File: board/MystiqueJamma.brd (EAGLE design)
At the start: 120 x 145 mm, 36 parts, among them IC1 7805, IC2 74LS245N, IC3 74LS245N, IC4 74LS245N, IC5 CY7C1049CV33

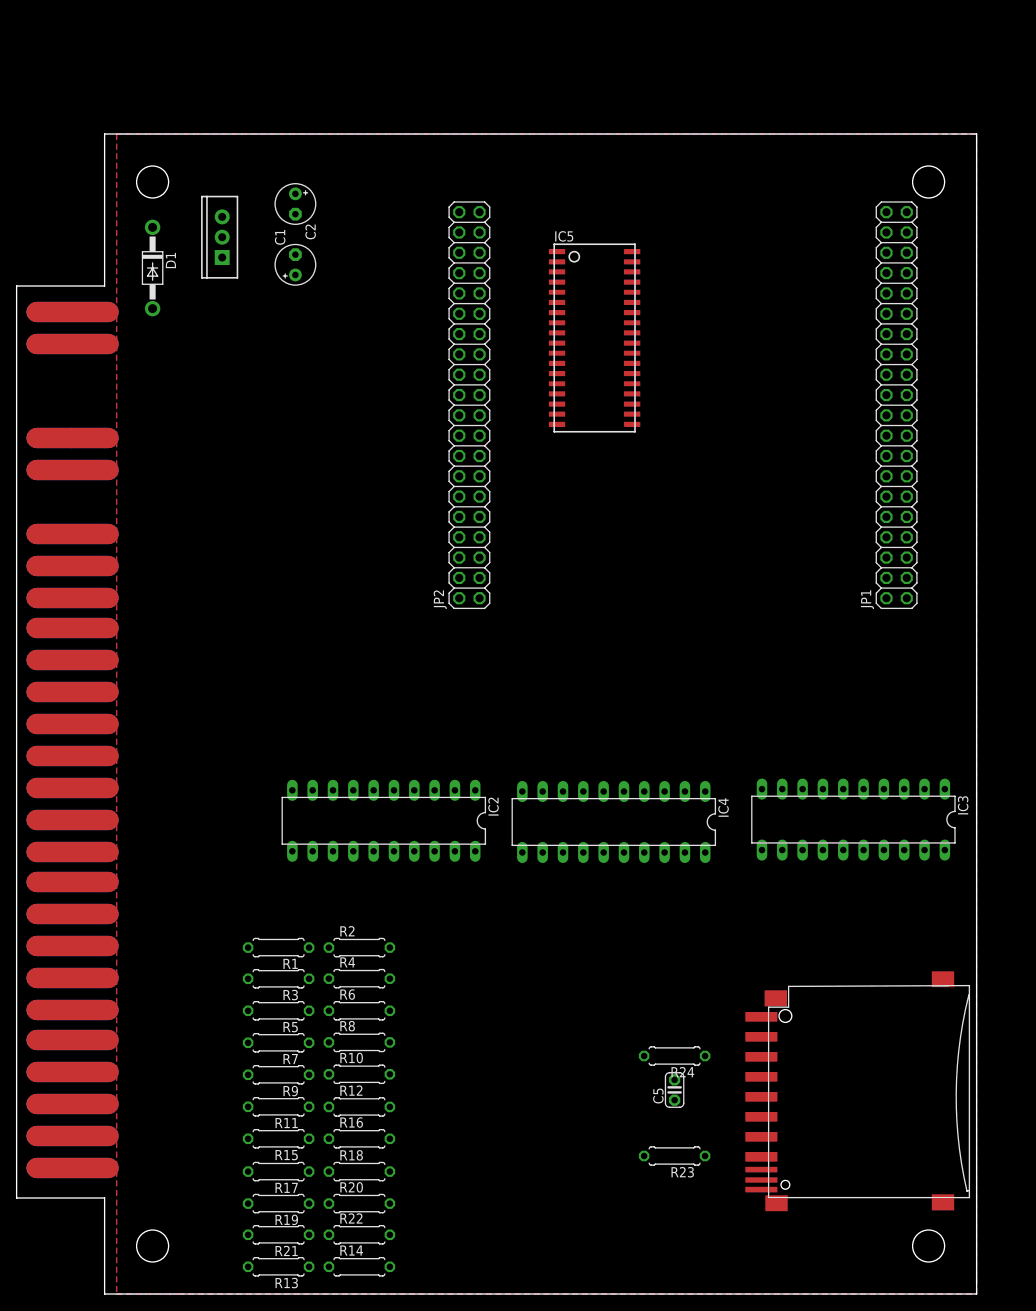
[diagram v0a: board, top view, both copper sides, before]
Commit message: changed the jamma connector and included audio TDA1543
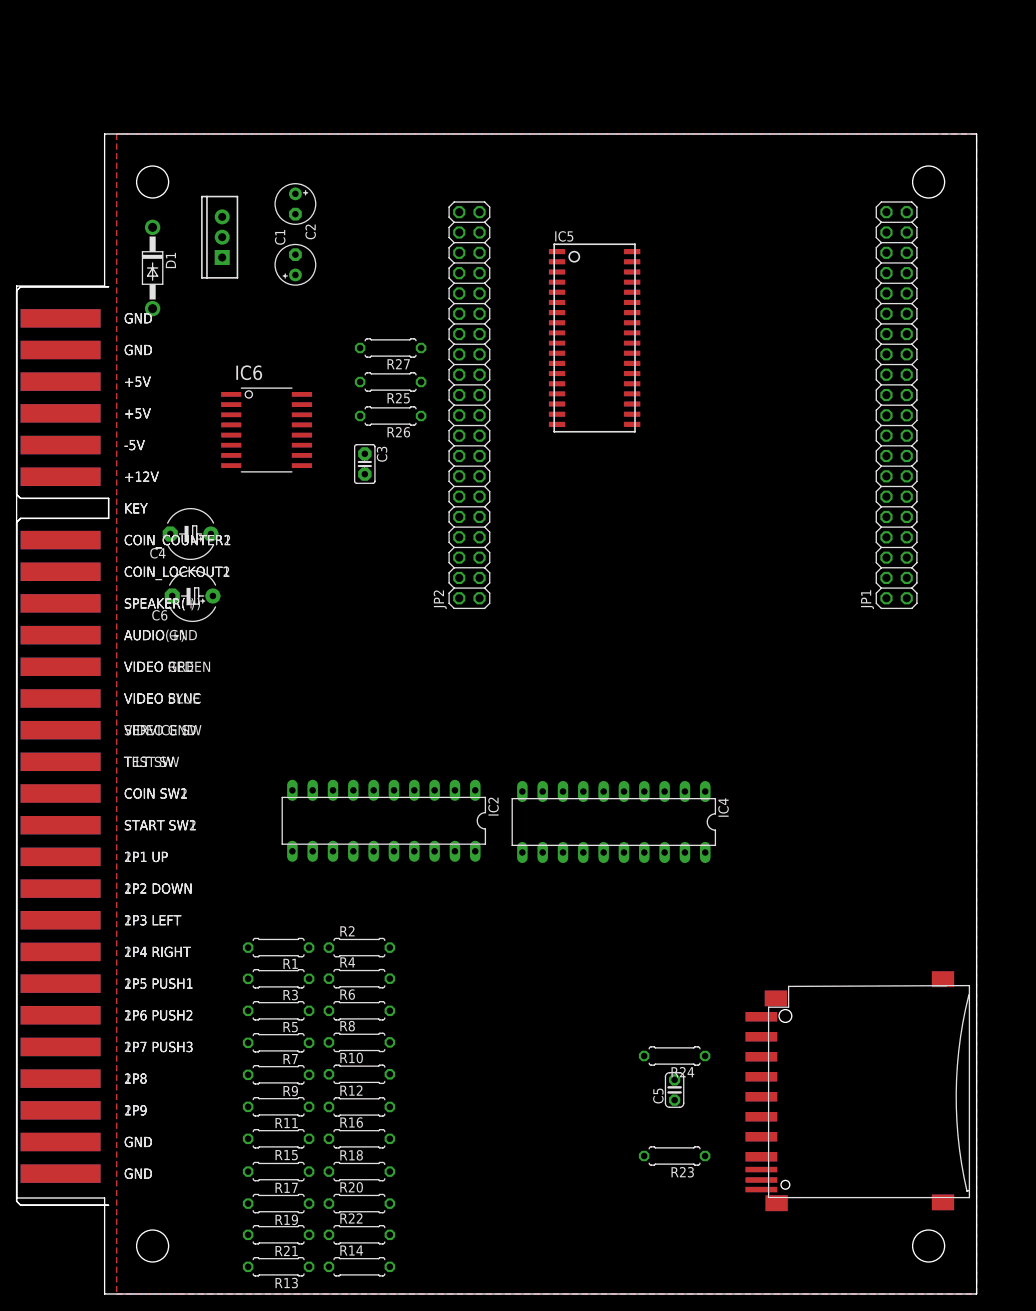
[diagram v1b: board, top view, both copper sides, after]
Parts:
- removed IC3: 74LS245N, 74xx-us:DIL20
- added C3: 100nF, adafruit:C025-025X050
- added C4, C6: 4.7uF, adafruit:E5-6
- added IC6: TDA1543T, TDA1543:SOIC-16NW
- added JAMMA1: JAMMA_TOP, JAMMA:JAMMA_TOP
- added JAMMA2: JAMMA_BOTTOM, JAMMA:JAMMA_BOTTOM
- added R25: 1k, adafruit:0207/7
- added R26, R27: 2k, adafruit:0207/7
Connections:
- removed net CS2_: IC3.18
- removed net CS2_3V: IC3.2
- removed net P2B1_: IC3.12
- removed net P2B1_3V: IC3.8
- removed net P2B2_: IC3.11
- removed net P2B2_3V: IC3.9
- removed net P2B3_: IC4.15
- removed net P2B3_3V: IC4.5
- removed net P2B4_: IC4.14
- removed net P2B4_3V: IC4.6
- removed net P2B5_: IC4.13
- removed net P2B5_3V: IC4.7
- removed net P2D_: IC3.15
- removed net P2D_3V: IC3.5
- removed net P2L_: IC3.14
- removed net P2L_3V: IC3.6
- removed net P2R_: IC3.13
- removed net P2R_3V: IC3.7
- removed net P2S_: IC3.17
- removed net P2S_3V: IC3.3
- removed net P2U_: IC3.16
- removed net P2U_3V: IC3.4
- new net +5V: JAMMA1.3, JAMMA1.4, JAMMA2.C, JAMMA2.D
- new net -5V: JAMMA1.5, JAMMA2.E
- new net 12+: JAMMA2.F
- new net DAC_DATA: IC6.5
- new net DAC_FSYNC: IC6.4
- new net DAC_SCK: IC6.3
- new net DAC_VREF: IC6.13, R25.2
- new net L_A: C6.+, IC6.12, R26.2
- new net L_AUDIO: C6.-
- new net R_A: C4.+, IC6.14, R27.2
- new net R_AUDIO: C4.-
- net +12: now also JAMMA1.6
- net +3V3: no longer IC3.20
- net +5REG: now also C3.1, IC6.11
- net COINSW1: now also JAMMA1.16
- net GND: now also C3.2, IC6.6, JAMMA1.1, JAMMA1.2, JAMMA1.27, JAMMA1.28, JAMMA2.A, JAMMA2.B, JAMMA2._E, JAMMA2._F, R25.1, R26.1, R27.1; no longer IC3.1, IC3.10, IC3.19
- net P1B1: now also JAMMA1.22
- net P1B2: now also JAMMA1.23
- net P1B3: now also JAMMA1.24
- net P1B4: now also JAMMA1.25
- net P1B5: now also JAMMA1.26
- net P1DW: now also JAMMA1.19
- net P1LH: now also JAMMA1.20
- net P1RH: now also JAMMA1.21
- net P1START: now also JAMMA1.17
- net P1UP: now also JAMMA1.18
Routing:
- net GND: track 72.0 -> 0.00 mm
- net -5: track 18.0 -> 0.00 mm
- net +12: track 18.0 -> 0.00 mm
- net VIDEOSYN: track 9.00 -> 0.00 mm
- net VIDEORED: track 9.00 -> 0.00 mm
- net VIDEOGR: track 9.00 -> 0.00 mm
- net VIDEOGND: track 9.00 -> 0.00 mm
- net VIDEOBLUE: track 9.00 -> 0.00 mm
- net TILTSW: track 9.00 -> 0.00 mm
- net TESTSW: track 9.00 -> 0.00 mm
- net SPEAKER-: track 9.00 -> 0.00 mm
- net SPEAKER+: track 9.00 -> 0.00 mm
- net SERVSW: track 9.00 -> 0.00 mm
- net S$11: track 9.00 -> 0.00 mm
- net P2UP: track 9.00 -> 0.00 mm
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
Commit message: audio circuit update
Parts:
- added R28, R29: 1k, adafruit:0207/7
- moved C4 14.3 mm to (34.8, 89.0)
- moved C6 14.2 mm to (35.0, 81.5)
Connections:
- new net JAMMA_SPK+: JAMMA1.10, R28.2, R29.2
- net GND: now also JAMMA2.L
- net L_AUDIO: now also R29.1
- net R_AUDIO: now also R28.1
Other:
- outline, holes or cut-outs redrawn
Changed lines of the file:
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@@
 <board>
 <plain>
-<wire x1="0" y1="12" x2="0" y2="126" width="0.1524" layer="20"/>
-<wire x1="11" y1="145" x2="120" y2="145" width="0.1524" layer="20"/>
+<wire x1="0" y1="11" x2="0" y2="126" width="0.1524" layer="20"/>
+<wire x1="11.5" y1="145" x2="120" y2="145" width="0.1524" layer="20"/>
 <wire x1="120" y1="145" x2="120" y2="0" width="0.1524" layer="20"/>
-<wire x1="120" y1="0" x2="11" y2="0" width="0.1524" layer="20"/>
-<wire x1="11" y1="0" x2="11" y2="12" width="0.1524" layer="20"/>
-<wire x1="11" y1="12" x2="0" y2="12" width="0.1524" layer="20"/>
-<wire x1="0" y1="126" x2="11" y2="126" width="0.1524" layer="20"/>
-<wire x1="11" y1="126" x2="11" y2="145" width="0.1524" layer="20"/>
+<wire x1="120" y1="0" x2="11.5" y2="0" width="0.1524" layer="20"/>
+<wire x1="11.5" y1="0" x2="11.5" y2="11" width="0.1524" layer="20"/>
+<wire x1="11.5" y1="11" x2="0" y2="11" width="0.1524" layer="20"/>
+<wire x1="0" y1="126" x2="11.5" y2="126" width="0.1524" layer="20"/>
+<wire x1="11.5" y1="126" x2="11.5" y2="145" width="0.1524" layer="20"/>
 <hole x="17" y="6" drill="4"/>
 <hole x="114" y="6" drill="4"/>
@@
 <element name="C3" library="adafruit" package="C025-025X050" value="100nF" x="43.5242" y="103.75" rot="R270"/>
 <element name="R27" library="adafruit" package="0207/7" value="2k" x="46.75" y="118.25" rot="R180"/>
-<element name="C4" library="adafruit" package="E5-6" value="4.7uF" x="21.75" y="95" rot="R180"/>
-<element name="C6" library="adafruit" package="E5-6" value="4.7uF" x="22" y="87.25" rot="R180"/>
+<element name="C4" library="adafruit" package="E5-6" value="4.7uF" x="34.75" y="89" rot="R180"/>
+<element name="C6" library="adafruit" package="E5-6" value="4.7uF" x="35" y="81.5" rot="R180"/>
 <element name="JAMMA1" library="JAMMA" package="JAMMA_TOP" value="JAMMA_TOP" x="5.5" y="68.5" rot="R270"/>
 <element name="JAMMA2" library="JAMMA" package="JAMMA_BOTTOM" value="JAMMA_BOTTOM" x="5.5" y="68.5" rot="R270"/>
+<element name="R28" library="adafruit" package="0207/7" value="1k" x="22.25" y="86.75" rot="R180"/>
+<element name="R29" library="adafruit" package="0207/7" value="1k" x="22.25" y="83.25" rot="R180"/>
 </elements>
 <signals>
@@
 <contactref element="JAMMA1" pad="27"/>
 <contactref element="JAMMA1" pad="28"/>
+<contactref element="JAMMA2" pad="L"/>
+<wire x1="108.73" y1="114.91" x2="111.27" y2="114.91" width="0" layer="19" extent="1-1"/>
+<wire x1="76.949" y1="120.135" x2="108.73" y2="114.91" width="0" layer="19" extent="1-1"/>
+<wire x1="67.551" y1="118.865" x2="76.949" y2="120.135" width="0" layer="19" extent="1-1"/>
+<wire x1="57.87" y1="114.91" x2="67.551" y2="118.865" width="0" layer="19" extent="1-1"/>
+<wire x1="55.33" y1="114.91" x2="57.87" y2="114.91" width="0" layer="19" extent="1-1"/>
+<wire x1="50.56" y1="114" x2="55.33" y2="114.91" width="0" layer="19" extent="1-1"/>
+<wire x1="50.56" y1="118.25" x2="50.56" y2="114" width="0" layer="19" extent="1-1"/>
+<wire x1="50.56" y1="109.75" x2="50.56" y2="114" width="0" layer="19" extent="1-1"/>
+<wire x1="43.5242" y1="102.48" x2="50.56" y2="109.75" width="0" layer="19" extent="1-1"/>
+<wire x1="26.835" y1="106.095" x2="43.5242" y2="102.48" width="0" layer="19" extent="1-1"/>
+<wire x1="34.85" y1="129.92" x2="50.56" y2="118.25" width="0" layer="19" extent="1-1"/>
+<wire x1="34.85" y1="134.98" x2="34.85" y2="129.92" width="0" layer="19" extent="1-1"/>
+<wire x1="25.7" y1="132.1" x2="34.85" y2="129.92" width="0" layer="19" extent="1-1"/>
+<wire x1="5.5" y1="121.96" x2="25.7" y2="132.1" width="0" layer="19" extent="1-1"/>
 <wire x1="5.5" y1="121.96" x2="5.5" y2="121.96" width="0" layer="19" extent="1-16"/>
 <wire x1="5.5" y1="118" x2="5.5" y2="121.96" width="0" layer="19" extent="1-1"/>
 <wire x1="5.5" y1="118" x2="5.5" y2="118" width="0" layer="19" extent="1-16"/>
-<wire x1="25.7" y1="132.1" x2="5.5" y2="121.96" width="0" layer="19" extent="1-1"/>
+<wire x1="5.5" y1="86.32" x2="26.835" y2="106.095" width="0" layer="19" extent="1-16"/>
+<wire x1="34.47" y1="62.96" x2="5.5" y2="86.32" width="0" layer="19" extent="16-16"/>
+<wire x1="54.79" y1="55.34" x2="34.47" y2="62.96" width="0" layer="19" extent="1-1"/>
+<wire x1="57.33" y1="62.96" x2="54.79" y2="55.34" width="0" layer="19" extent="1-1"/>
+<wire x1="63.22" y1="62.81" x2="57.33" y2="62.96" width="0" layer="19" extent="1-1"/>
+<wire x1="83.54" y1="55.19" x2="63.22" y2="62.81" width="0" layer="19" extent="1-1"/>
+<wire x1="86.08" y1="62.81" x2="83.54" y2="55.19" width="0" layer="19" extent="1-1"/>
+<wire x1="82.25" y1="26.77" x2="83.54" y2="55.19" width="0" layer="19" extent="1-1"/>
+<wire x1="93.1" y1="27.15" x2="82.25" y2="26.77" width="0" layer="19" extent="1-1"/>
+<wire x1="93.1" y1="19.65" x2="93.1" y2="27.15" width="0" layer="19" extent="1-1"/>
+<wire x1="115.8" y1="11.45" x2="93.1" y2="19.65" width="0" layer="19" extent="1-1"/>
 <wire x1="5.5" y1="19" x2="34.47" y2="62.96" width="0" layer="19" extent="16-16"/>
 <wire x1="5.5" y1="19" x2="5.5" y2="19" width="0" layer="19" extent="1-16"/>
@@
 <contactref element="C6" pad="+"/>
 <wire x1="35.665" y1="107.365" x2="42.94" y2="109.75" width="0" layer="19" extent="1-1"/>
-<wire x1="24.54" y1="87.25" x2="35.665" y2="107.365" width="0" layer="19" extent="1-1"/>
+<wire x1="37.54" y1="81.5" x2="35.665" y2="107.365" width="0" layer="19" extent="1-1"/>
 </signal>
 <signal name="R_A">
@@
 <contactref element="C4" pad="+"/>
 <wire x1="35.665" y1="109.905" x2="42.94" y2="118.25" width="0" layer="19" extent="1-1"/>
-<wire x1="24.29" y1="95" x2="35.665" y2="109.905" width="0" layer="19" extent="1-1"/>
+<wire x1="37.29" y1="89" x2="35.665" y2="109.905" width="0" layer="19" extent="1-1"/>
 </signal>
 <signal name="R_AUDIO">
 <contactref element="C4" pad="-"/>
+<contactref element="R28" pad="1"/>
+<wire x1="26.06" y1="86.75" x2="32.21" y2="89" width="0" layer="19" extent="1-1"/>
 </signal>
 <signal name="L_AUDIO">
 <contactref element="C6" pad="-"/>
+<contactref element="R29" pad="1"/>
+<wire x1="26.06" y1="83.25" x2="32.46" y2="81.5" width="0" layer="19" extent="1-1"/>
 </signal>
 <signal name="+5V">
@@
 <contactref element="JAMMA2" pad="F"/>
 </signal>
+<signal name="JAMMA_SPK+">
+<contactref element="JAMMA1" pad="10"/>
+<contactref element="R29" pad="2"/>
+<contactref element="R28" pad="2"/>
+<wire x1="18.44" y1="86.75" x2="5.5" y2="86.32" width="0" layer="19" extent="1-1"/>
+<wire x1="18.44" y1="83.25" x2="18.44" y2="86.75" width="0" layer="19" extent="1-1"/>
+</signal>
 </signals>

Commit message: audio circuit
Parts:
- added R30: 20k, adafruit:0207/7
- R28, R29: value 1k -> 470
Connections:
- net GND: now also R30.1
- net JAMMA_SPK+: now also R30.2
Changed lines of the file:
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@@
 <layer number="24" name="bOrigins" color="15" fill="1" visible="yes" active="yes"/>
 <layer number="25" name="tNames" color="7" fill="1" visible="yes" active="yes"/>
-<layer number="26" name="bNames" color="7" fill="1" visible="no" active="yes"/>
-<layer number="27" name="tValues" color="7" fill="1" visible="no" active="yes"/>
-<layer number="28" name="bValues" color="7" fill="1" visible="no" active="yes"/>
-<layer number="29" name="tStop" color="7" fill="3" visible="no" active="yes"/>
-<layer number="30" name="bStop" color="7" fill="6" visible="no" active="yes"/>
+<layer number="26" name="bNames" color="7" fill="1" visible="yes" active="yes"/>
+<layer number="27" name="tValues" color="7" fill="1" visible="yes" active="yes"/>
+<layer number="28" name="bValues" color="7" fill="1" visible="yes" active="yes"/>
+<layer number="29" name="tStop" color="7" fill="3" visible="yes" active="yes"/>
+<layer number="30" name="bStop" color="7" fill="6" visible="yes" active="yes"/>
 <layer number="31" name="tCream" color="7" fill="4" visible="yes" active="yes"/>
-<layer number="32" name="bCream" color="7" fill="5" visible="no" active="yes"/>
-<layer number="33" name="tFinish" color="6" fill="3" visible="no" active="yes"/>
-<layer number="34" name="bFinish" color="6" fill="6" visible="no" active="yes"/>
+<layer number="32" name="bCream" color="7" fill="5" visible="yes" active="yes"/>
+<layer number="33" name="tFinish" color="6" fill="3" visible="yes" active="yes"/>
+<layer number="34" name="bFinish" color="6" fill="6" visible="yes" active="yes"/>
 <layer number="35" name="tGlue" color="7" fill="4" visible="no" active="yes"/>
 <layer number="36" name="bGlue" color="7" fill="5" visible="no" active="yes"/>
@@
 <element name="JAMMA1" library="JAMMA" package="JAMMA_TOP" value="JAMMA_TOP" x="5.5" y="68.5" rot="R270"/>
 <element name="JAMMA2" library="JAMMA" package="JAMMA_BOTTOM" value="JAMMA_BOTTOM" x="5.5" y="68.5" rot="R270"/>
-<element name="R28" library="adafruit" package="0207/7" value="1k" x="22.25" y="86.75" rot="R180"/>
-<element name="R29" library="adafruit" package="0207/7" value="1k" x="22.25" y="83.25" rot="R180"/>
+<element name="R28" library="adafruit" package="0207/7" value="470" x="22.25" y="86.75" rot="R180"/>
+<element name="R29" library="adafruit" package="0207/7" value="470" x="22.25" y="83.25" rot="R180"/>
+<element name="R30" library="adafruit" package="0207/7" value="20k" x="22.25" y="79.75" rot="R180"/>
 </elements>
 <signals>
@@
 <contactref element="JAMMA1" pad="28"/>
 <contactref element="JAMMA2" pad="L"/>
-<wire x1="108.73" y1="114.91" x2="111.27" y2="114.91" width="0" layer="19" extent="1-1"/>
-<wire x1="76.949" y1="120.135" x2="108.73" y2="114.91" width="0" layer="19" extent="1-1"/>
-<wire x1="67.551" y1="118.865" x2="76.949" y2="120.135" width="0" layer="19" extent="1-1"/>
-<wire x1="57.87" y1="114.91" x2="67.551" y2="118.865" width="0" layer="19" extent="1-1"/>
-<wire x1="55.33" y1="114.91" x2="57.87" y2="114.91" width="0" layer="19" extent="1-1"/>
-<wire x1="50.56" y1="114" x2="55.33" y2="114.91" width="0" layer="19" extent="1-1"/>
-<wire x1="50.56" y1="118.25" x2="50.56" y2="114" width="0" layer="19" extent="1-1"/>
-<wire x1="50.56" y1="109.75" x2="50.56" y2="114" width="0" layer="19" extent="1-1"/>
-<wire x1="43.5242" y1="102.48" x2="50.56" y2="109.75" width="0" layer="19" extent="1-1"/>
-<wire x1="26.835" y1="106.095" x2="43.5242" y2="102.48" width="0" layer="19" extent="1-1"/>
-<wire x1="34.85" y1="129.92" x2="50.56" y2="118.25" width="0" layer="19" extent="1-1"/>
-<wire x1="34.85" y1="134.98" x2="34.85" y2="129.92" width="0" layer="19" extent="1-1"/>
-<wire x1="25.7" y1="132.1" x2="34.85" y2="129.92" width="0" layer="19" extent="1-1"/>
-<wire x1="5.5" y1="121.96" x2="25.7" y2="132.1" width="0" layer="19" extent="1-1"/>
+<contactref element="R30" pad="1"/>
 <wire x1="5.5" y1="121.96" x2="5.5" y2="121.96" width="0" layer="19" extent="1-16"/>
 <wire x1="5.5" y1="118" x2="5.5" y2="121.96" width="0" layer="19" extent="1-1"/>
 <wire x1="5.5" y1="118" x2="5.5" y2="118" width="0" layer="19" extent="1-16"/>
-<wire x1="5.5" y1="86.32" x2="26.835" y2="106.095" width="0" layer="19" extent="1-16"/>
-<wire x1="34.47" y1="62.96" x2="5.5" y2="86.32" width="0" layer="19" extent="16-16"/>
-<wire x1="54.79" y1="55.34" x2="34.47" y2="62.96" width="0" layer="19" extent="1-1"/>
-<wire x1="57.33" y1="62.96" x2="54.79" y2="55.34" width="0" layer="19" extent="1-1"/>
-<wire x1="63.22" y1="62.81" x2="57.33" y2="62.96" width="0" layer="19" extent="1-1"/>
-<wire x1="83.54" y1="55.19" x2="63.22" y2="62.81" width="0" layer="19" extent="1-1"/>
-<wire x1="86.08" y1="62.81" x2="83.54" y2="55.19" width="0" layer="19" extent="1-1"/>
-<wire x1="82.25" y1="26.77" x2="83.54" y2="55.19" width="0" layer="19" extent="1-1"/>
-<wire x1="93.1" y1="27.15" x2="82.25" y2="26.77" width="0" layer="19" extent="1-1"/>
-<wire x1="93.1" y1="19.65" x2="93.1" y2="27.15" width="0" layer="19" extent="1-1"/>
-<wire x1="115.8" y1="11.45" x2="93.1" y2="19.65" width="0" layer="19" extent="1-1"/>
+<wire x1="25.7" y1="132.1" x2="5.5" y2="121.96" width="0" layer="19" extent="1-1"/>
+<wire x1="5.5" y1="86.32" x2="26.06" y2="79.75" width="0" layer="19" extent="16-16"/>
 <wire x1="5.5" y1="19" x2="34.47" y2="62.96" width="0" layer="19" extent="16-16"/>
 <wire x1="5.5" y1="19" x2="5.5" y2="19" width="0" layer="19" extent="1-16"/>
@@
 <contactref element="R29" pad="2"/>
 <contactref element="R28" pad="2"/>
-<wire x1="18.44" y1="86.75" x2="5.5" y2="86.32" width="0" layer="19" extent="1-1"/>
+<contactref element="R30" pad="2"/>
 <wire x1="18.44" y1="83.25" x2="18.44" y2="86.75" width="0" layer="19" extent="1-1"/>
+<wire x1="18.44" y1="79.75" x2="18.44" y2="83.25" width="0" layer="19" extent="1-1"/>
+<wire x1="5.5" y1="86.32" x2="18.44" y2="86.75" width="0" layer="19" extent="1-1"/>
 </signal>
 </signals>

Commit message: video circuit
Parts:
- added R31, R32, R33, R34, R35, R39, R40, R41, R42, R43, R47, R48, R49, R50, R51: 2k, adafruit:0207/7
- added R36, R37, R38, R44, R45, R46, R52, R53, R54: 1k, adafruit:0207/7
- added R55, R56, R57: 220, adafruit:0207/7
- added X1: (no value), adafruit:HDF15H
- moved IC4 43.9 mm to (58.5, 18.1), turned to 270 degrees
- moved IC2 8.87 mm to (39.1, 53.4)
- moved C3 3.38 mm to (46.8, 104.8), turned to 0 degrees
- moved C4 0.12 mm to (34.9, 89.0)
- moved C6 0.12 mm to (34.9, 81.5)
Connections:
- new net JVIDEO_BLUE: JAMMA1.13, R55.2
- new net JVIDEO_GREEN: JAMMA2.N, R56.2
- new net JVIDEO_RED: JAMMA1.12, R57.2
- new net N$1: R31.1, R32.1, R36.2
- new net N$10: R42.1, R45.1, R46.2
- new net N$11: R47.1, R48.1, R52.2
- new net N$12: R49.1, R52.1, R53.2
- new net N$13: R50.1, R53.1, R54.2
- new net N$3: R33.1, R36.1, R37.2
- new net N$4: X1.8
- new net N$5: X1.7
- new net N$6: X1.6
- new net N$7: R34.1, R37.1, R38.2
- new net N$8: R39.1, R40.1, R44.2
- new net N$9: R41.1, R44.1, R45.2
- new net VGA_B0: R47.2
- new net VGA_B1: R49.2
- new net VGA_B2: R50.2
- new net VGA_B3: R51.2
- new net VGA_BLUE: R51.1, R54.1, R55.1, X1.3
- new net VGA_G0: R39.2
- new net VGA_G1: R41.2
- new net VGA_G2: R42.2
- new net VGA_G3: R43.2
- new net VGA_GREEN: R43.1, R46.1, R56.1, X1.2
- new net VGA_HSYNC: JAMMA2.P, X1.13
- new net VGA_R0: R31.2
- new net VGA_R1: R33.2
- new net VGA_R2: R34.2
- new net VGA_R3: R35.2
- new net VGA_RED: R35.1, R38.1, R57.1, X1.1
- new net VGA_VSYNC: X1.14
- net GND: now also JAMMA1.14, R32.2, R40.2, R48.2, X1.10, X1.5
